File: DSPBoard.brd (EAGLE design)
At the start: 416 x 128.5 mm, 454 parts, among them IC1 AD1939WBSTZ, IC10 LM833D, IC11 LM833D, IC12 TL074D, IC13 4520D, IC2 24AA1025, IC29 TL074D, IC3 LM4040B10DBZ, IC4 LM833D, IC5 LM833D, IC6 LM833D, IC7 LM833D, IC8 LM833D, IC9 LM833D, U1 LM11173.3NOPB, U2 PEC11R-4315F-N0012, U3 PEC11R-4315F-N0012, X1 2510-, Y1 12.288MHz

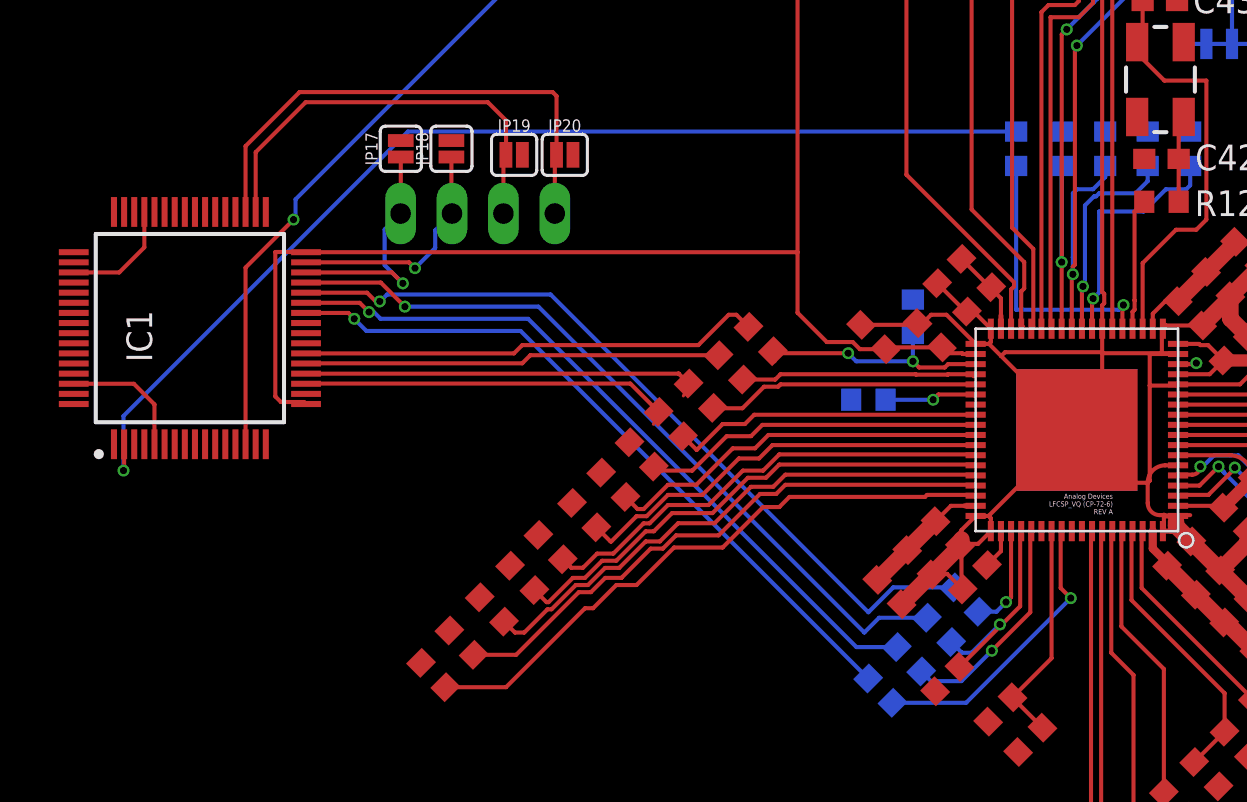
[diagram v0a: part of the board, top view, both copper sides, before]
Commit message: rerouteclockreccomendataions
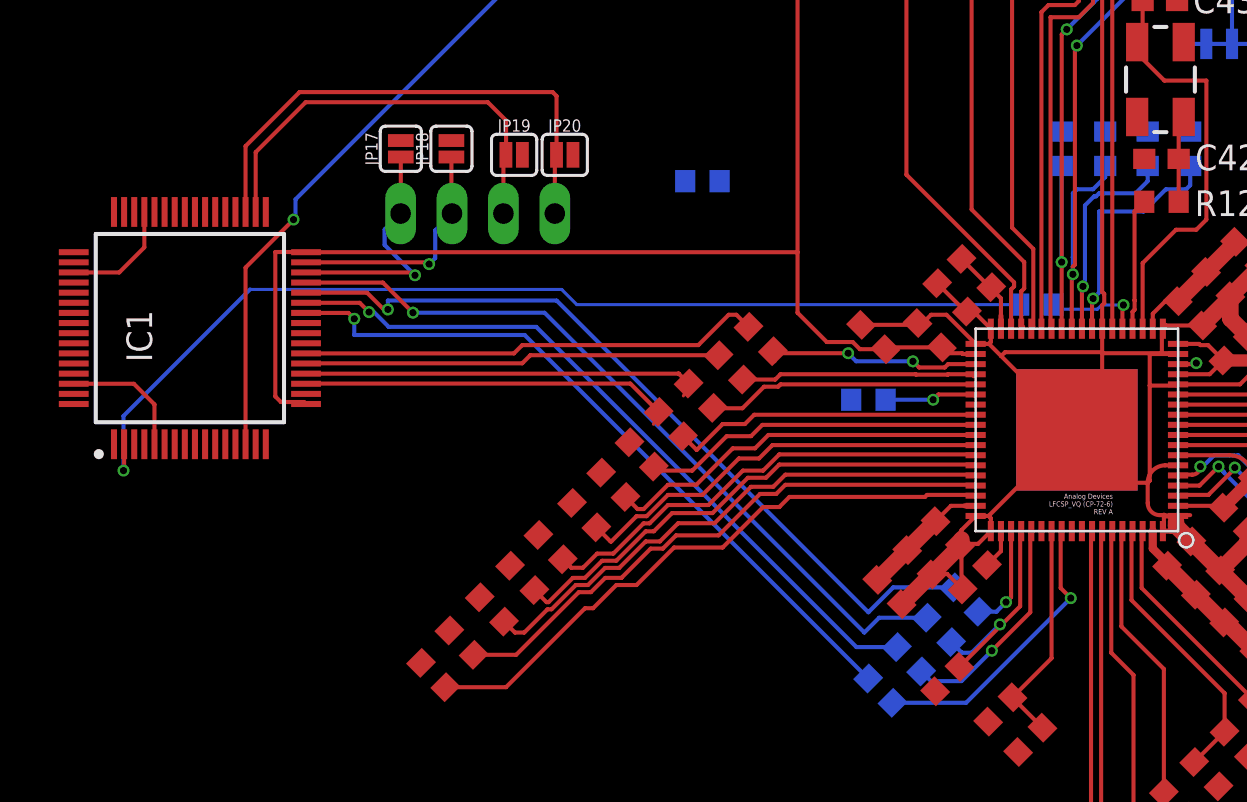
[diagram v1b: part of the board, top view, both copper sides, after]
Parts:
- moved R170 12.4 mm to (189.3, 74.0), turned to 180 degrees
- moved R180 7.76 mm to (205.8, 67.9), turned to 0 degrees
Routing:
- net N$141: track 13.7 -> 4.82 mm
- net 1452_CLK_OUT: track 53.9 -> 51.2 mm
- net MP4: track 12.4 -> 11.0 mm

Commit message: relayingThechips
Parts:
- moved R155 68.9 mm to (108.3, 36.5), turned to 90 degrees
- moved R154 68.5 mm to (110.4, 36.6), turned to 90 degrees
- moved R56 68.2 mm to (112.7, 36.7), turned to 90 degrees
- moved R26 67.9 mm to (114.8, 36.8), turned to 90 degrees
- moved R25 67.7 mm to (116.9, 36.8), turned to 90 degrees
- moved R24 67.5 mm to (119.2, 36.8), turned to 90 degrees
- moved R167 67.4 mm to (121.3, 36.8), turned to 270 degrees
- moved R175 54.8 mm to (152.6, 28.6), turned to 90 degrees
- moved R156 54.4 mm to (154.7, 28.6), turned to 270 degrees
- moved R161 54.1 mm to (156.8, 28.6), turned to 90 degrees
- moved R176 53.8 mm to (159.0, 28.6), turned to 90 degrees
- moved R159 53.6 mm to (161.1, 28.7), turned to 270 degrees
- moved R157 53.4 mm to (163.3, 28.7), turned to 270 degrees
- moved R160 53.3 mm to (165.4, 28.7), turned to 90 degrees
- moved R158 53.1 mm to (167.5, 28.8), turned to 270 degrees
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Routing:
- net N$28: track 21.5 -> 206.3 mm
- net MP0: track 11.9 -> 75.9 mm, vias 1 -> 0
- net +3V3: track 124.0 -> 64.0 mm
- net S_SDA: track 50.6 -> 104.6 mm
- net 1452_CLK_OUT: track 51.2 -> 0.29 mm, vias 1 -> 0
- net N$27: track 6.51 -> 55.8 mm
- net RESET: track 108.1 -> 59.3 mm, vias 2 -> 1
- net ASDATA2: track 35.7 -> 4.18 mm, vias 1 -> 0
- net ALRCLK: track 38.1 -> 10.3 mm
- net ABCLK: track 39.7 -> 13.1 mm
- net S_AUX_ADC1: track 27.9 -> 54.3 mm
- net N$134: track 30.2 -> 3.83 mm
- net ASDATA1: track 36.2 -> 10.3 mm, vias 1 -> 0
- net N$132: track 28.3 -> 4.23 mm
- net S_AUX_ADC0: track 31.1 -> 54.7 mm
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
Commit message: board update
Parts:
- moved R180 16.7 mm to (175.2, 49.1)
- moved R8 14.2 mm to (165.2, 55.9)
- moved R6 14.1 mm to (161.3, 55.5)
- moved R7 12.9 mm to (163.3, 55.9)
- moved R11 10.9 mm to (162.3, 52.6)
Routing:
- net 1452_CLK_OUT: track 0.29 -> 30.7 mm, vias 0 -> 1
- net MP10: track 11.3 -> 20.8 mm
- net N$76: track 5.24 -> 13.7 mm
- net N$35: track 14.5 -> 18.6 mm
- net ASDATA1: track 10.3 -> 13.9 mm, vias 0 -> 1
- net N$120: track 11.0 -> 12.7 mm
- net N$141: track 0.32 -> 1.89 mm, vias 0 -> 1
- net ALRCLK: track 10.3 -> 11.3 mm, vias 1 -> 2
- net ASDATA2: track 4.18 -> 3.33 mm, vias 0 -> 1
- net ABCLK: track 13.1 -> 12.9 mm, vias 1 -> 2

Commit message: continuing to layout
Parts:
- removed SV2: (no value), con-lstb:MA04-1
- added TP1, TP2, TP3, TP4: TESTPAD_TPSQTP16R, BeagleBone_Blue_R3:TESTPAD_TP16R
- moved C119 379.8 mm to (152.6, 77.6), flipped to the bottom, turned to 270 degrees
- moved C98 366.6 mm to (345.5, 180.0)
- moved R70 364.8 mm to (347.4, 172.4)
- moved C96 360.8 mm to (344.7, 178.5)
- moved R99 360.8 mm to (337.0, 165.8)
- moved C52 360.8 mm to (324.3, 165.8)
- moved C63 360.8 mm to (318.0, 165.8)
- moved C67 360.8 mm to (330.7, 159.4)
- moved C74 360.8 mm to (311.6, 165.8)
- moved C78 360.8 mm to (318.0, 159.4)
- moved C83 360.8 mm to (311.6, 159.4)
- moved R72 360.8 mm to (330.7, 172.1)
- moved R73 360.8 mm to (324.3, 172.1)
- moved R74 360.8 mm to (318.0, 172.1)
- moved R76 360.8 mm to (311.6, 172.1)
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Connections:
- net +3V3: no longer D1.1, D2.2, D3.1, D4.2, D5.1, D6.2, D7.1, D8.2
- net 3V3A: now also D1.1, D2.2, D3.1, D4.2, D5.1, D6.2, D7.1, D8.2
- net N$135: now also TP4.TP; no longer SV2.1
- net N$158: now also TP3.TP; no longer SV2.2
- net N$159: now also TP2.TP; no longer SV2.3
- net N$7: now also TP1.TP; no longer SV2.4
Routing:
- net N$28: track 206.3 -> 9.04 mm
- net AIN0+: track 0.00 -> 111.1 mm, vias 0 -> 1
- net AIN0-: track 0.00 -> 108.7 mm, vias 0 -> 1
- net S_SDA: track 104.6 -> 2.01 mm, vias 0 -> 1
- net MP0: track 75.9 -> 12.8 mm, vias 0 -> 1
- net S_AUX_ADC0: track 54.7 -> 7.85 mm
- net S_AUX_ADC1: track 54.3 -> 7.51 mm
- net RESET: track 59.3 -> 103.5 mm, vias 1 -> 2
- net GND: track 217.6 -> 261.5 mm, vias 10 -> 35
- net +3V3: track 64.0 -> 107.2 mm, vias 3 -> 5
- net S_SCL: track 39.9 -> 1.46 mm, vias 0 -> 1
- net N$27: track 55.8 -> 17.9 mm
- net 3V3A: track 0.00 -> 28.0 mm, vias 0 -> 2
- net N$134: track 3.83 -> 15.9 mm, vias 0 -> 1
- net N$132: track 4.23 -> 15.4 mm, vias 0 -> 1
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
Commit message: MAybe I need to rethink this
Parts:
- removed C100, C102, C103, C104, C106, C99: 1nf, rcl:C0603
- removed C101, C105, C56: 10nF, rcl:C0603
- removed C107, C108: 100nF, rcl:C0603
- removed C17, C25: 100nf, rcl:C0603
- removed C50: 220uF, rcl:PANASONIC_D
- removed C51: 1nF, rcl:C0603
- removed C52: 470p, rcl:C0603
- removed C53: 1uF, rcl:C0603
- removed C54: 100uF, rcl:PANASONIC_D
- removed C55: 100pF, rcl:C0603
- removed D3, D4, D7, D8: BAV99,215, SamacSys_Parts:SOT95P230X110-3N
- removed IC10, IC5: LM833D, linear:SO08
- removed JP10, JP14, JP15, JP16, JP4, JP5, JP6, JP7, JP8, JP9: JUMPER-SMT_2_NC_PASTE_SILK, SparkFun-Jumpers:SMT-JUMPER_2_NC_PASTE_SILK
- removed R103, R114: 100R, rcl:R0603
- removed R104, R106, R115, R117, R118, R120, R121, R123, R67: 2.2k, rcl:R0603
- removed R105, R116, R119, R122: 68R, rcl:R0603
- removed R164, R165, R166, R167, R168, R169, R170, R171, R172, R173, R174, R175, R176, R53: 33R, rcl:R0603
- removed R183, R184, R185: 100, rcl:R0603
- removed R46: 6k2, rcl:R0603
- removed R47, R48: 22R, rcl:R0603
- removed R49: 18k, rcl:R0603
- removed TP1, TP2, TP3, TP4: TESTPAD_TPSQTP16R, BeagleBone_Blue_R3:TESTPAD_TP16R
- removed U$14, U$15, U$7: WQP-PJ301M-12_JACK, thonkiconn:WQP-PJ301M-12_JACK
- removed U$24: PHOTON_SMD, Particle-Devices:PHOTON_SMD
- added C133, C180: 1nF, rcl:C0603
- added C156, C181: 470p, rcl:C0603
- added C162, C182: 1uF, rcl:C0603
- added C163, C183: 100uF, rcl:PANASONIC_D
- added C164, C166, C184, C186: 100pF, rcl:C0603
- added C165, C185, C69: 10nF, rcl:C0603
- added C177, C178, C58: 100nf, rcl:C0603
- added C179: 220uF, rcl:PANASONIC_D
- added D10, D13, D14, D9: BAV99,215, SamacSys_Parts:SOT95P230X110-3N
- added IC14, IC16: LM833D, linear:SO08
- added LED1, LED2, LED3, LED4, LED5, LED6, LED7, LED8: (no value), led:CHIPLED_0805
- added R186, R208: 18k, rcl:R0603
- added R187, R209: 2.7k, rcl:R0603
- added R188, R189, R210, R211: 2.2k, rcl:R0603
- added R190, R212: 12.7k, rcl:R0603
- added R191, R192, R213, R214: 10k, rcl:R0603
- added R193, R215: 6k2, rcl:R0603
- added R194, R195, R216, R217: 22R, rcl:R0603
- added R196, R218: 100, rcl:R0603
- added U$22, U$30, U$31: WQP-PJ301M-12_JACK, thonkiconn:WQP-PJ301M-12_JACK
- C132: value 100pF -> 220uF; device rcl:C0603 -> rcl:PANASONIC_D
- C57, C77: value 100pF -> 100nf
- C59: value 100nf -> 220uF; device rcl:C0603 -> rcl:PANASONIC_D
- C60: value 100nf -> 1nF
- C61: value 220uF -> 470p; device rcl:PANASONIC_D -> rcl:C0603
- C62: value 1nF -> 1uF
- C63: value 470p -> 100uF; device rcl:C0603 -> rcl:PANASONIC_D
- C64: value 1uF -> 100pF
- C65: value 100uF -> 10nF; device rcl:PANASONIC_D -> rcl:C0603
- C67, C93: value 10nF -> 1nf
- C68: value 100pF -> 1nf
- C70, C71: value 100nf -> 1nf
- C72: value 220uF -> 1nf; device rcl:PANASONIC_D -> rcl:C0603
- C73: value 1nF -> 10nF
- C74: value 470p -> 1nf
- C75: value 1uF -> 100nF
- C76: value 100uF -> 100nF; device rcl:PANASONIC_D -> rcl:C0603
- C78: value 10nF -> 100nf
- C79, C80: value 100nF -> 1nf
- C91, C95: value 1nf -> 10nF
- C96: device rcl:C0805 -> rcl:C0603
- C97: value 10nF -> 100nF
- C98: value 1nf -> 100nF; device rcl:C0805 -> rcl:C0603
- R15: value 18k -> 33R
- R154: value 33R -> 100R
- R155, R159, R160, R163: value 33R -> 2.2k
- R158, R161: value 33R -> 68R
- R25: value 33R -> 10k
- R26, R29: value 33R -> 470
- R30: value 2.7k -> 470
- R32, R42: value 2.2k -> 470
- R43: value 12.7k -> 470
- R44, R45: value 10k -> 470
- R50: value 2.7k -> 18k
- R51: value 2.2k -> 2.7k
- R55, R69: value 12.7k -> 2.2k
- R57: value 10k -> 12.7k
- R62: value 6k2 -> 10k
- R63: value 22R -> 6k2
- R65: value 18k -> 22R
- R66: value 2.7k -> 100
- R68: value 2.2k -> 100R
- R70: value 10k -> 68R
- R71: value 10k -> 2.2k
- R72: value 6k2 -> 2.2k
- R73: value 22R -> 68R
- R74: value 22R -> 2.2k
- U$29: value PROTOTYPEAREA -> WQP-PJ301M-12_JACK; device audioic:PROTOTYPEAREA -> thonkiconn:WQP-PJ301M-12_JACK
- U$5: value WQP-PJ301M-12_JACK -> PHOTON_WITH_HEADERS; device thonkiconn:WQP-PJ301M-12_JACK -> Particle-Devices:PHOTON
- moved JP1 594.2 mm to (-217.9, -133.8)
- moved JP3 520.5 mm to (-226.5, -133.8), flipped to the top, turned to 0 degrees
- moved R45 472.1 mm to (226.5, -84.6)
- moved R44 464.1 mm to (226.5, -79.7)
- moved R15 425.2 mm to (276.1, -40.5)
- moved R42 418.8 mm to (226.5, -69.9)
- moved C95 409.9 mm to (174.7, 86.4), flipped to the bottom
- moved C94 407.2 mm to (177.9, 89.9), flipped to the bottom
- moved R95 401.2 mm to (169.6, 88.3), flipped to the bottom
- moved C110 397.1 mm to (192.6, 89.9), flipped to the bottom, turned to 180 degrees
- moved R32 395.8 mm to (226.5, -65.0)
- moved R93 395.6 mm to (168.9, 83.7), flipped to the bottom, turned to 90 degrees
- moved C92 393.7 mm to (169.9, 93.3), flipped to the bottom, turned to 180 degrees
- moved R153 390.7 mm to (194.4, 54.4), turned to 180 degrees
- moved C91 388.9 mm to (167.9, 86.2), flipped to the bottom, turned to 180 degrees
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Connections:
- removed net !RST: JP1.2, U$24.23, U$29.P$29
- removed net MP12: R156.1, R161.2, U$1.66
- removed net MP13: R157.1, R160.2, U$1.69
- removed net MP8: JP15.2, R166.2
- removed net MP9: JP16.2, R165.2
- removed net MUX1_X: JP3.2, JP9.1, MUX1.3, U$29.USER_PAD1237
- removed net MUX2_A_INH: MUX2.6, U$29.USER_PAD1249
- removed net MUX2_A_X: JP10.1, JP8.2, MUX2.3, U$29.USER_PAD1250
- removed net MUX2_A_X0: MUX2.13, U$29.USER_PAD1251
- removed net MUX2_A_X1: MUX2.14, U$29.USER_PAD1252
- removed net MUX2_A_X2: MUX2.15, U$29.USER_PAD1253
- removed net MUX2_A_X3: MUX2.12, U$29.USER_PAD1254
- removed net MUX2_A_X4: MUX2.1, U$29.USER_PAD1255
- removed net MUX2_A_X5: MUX2.5, U$29.USER_PAD1256
- removed net MUX2_A_X6: MUX2.2, U$29.USER_PAD1257
- removed net MUX2_A_X7: MUX2.4, U$29.USER_PAD1258
- removed net N$100: C141.1, IC11.5, R129.2
- removed net N$101: C138.2, R124.2, U$15.P$1
- removed net N$102: C109.2, R103.2, U$14.P$1
- removed net N$103: C110.1, IC11.1, R103.1, R104.2
- removed net N$140: R25.1, U$1.48
- removed net N$143: R160.1, U$29.P$28
- removed net N$144: R161.1, U$29.P$27
- removed net N$145: R163.1, U$29.P$26
- removed net N$146: R164.1, U$29.P$25
- removed net N$147: R165.1, U$29.P$24
- removed net N$148: R166.1, U$29.P$23
- removed net N$149: R167.1, U$29.P$22
- removed net N$150: R168.1, U$29.P$21
- removed net N$151: R169.1, U$29.P$20
- removed net N$152: R170.1, U$29.P$19
- removed net N$153: R171.1, U$29.P$18
- removed net N$154: R172.1, U$29.P$17
- removed net N$155: R173.1, U$29.P$16
- removed net N$156: R174.1, U$29.P$15
- removed net N$161: R185.2, R46.1
- removed net N$162: R183.2, R62.1
- removed net N$163: R184.2, R72.1
- removed net N$98: C140.2, R128.2, R129.1, R130.2
- removed net N$99: C139.1, IC11.7, R124.1, R125.2
- removed net P_ADC0: U$24.12, U$29.P$36
- removed net P_ADC1: U$24.11, U$29.P$37
- removed net P_ADC2: U$24.10, U$29.P$38
- removed net P_ADC3: U$24.9, U$29.P$39
- removed net P_ADC4: U$24.8, U$29.P$40
- removed net P_ADC5: U$24.7, U$29.P$41
- removed net P_ADC6_DAC: U$24.6, U$29.P$42
- removed net P_ADC7_WPK: U$24.5, U$29.P$43
- removed net P_D0: U$24.13, U$29.P$3
- removed net P_D1: U$24.14, U$29.P$4
- removed net P_D2: U$24.15, U$29.P$5
- removed net P_D3: U$24.16, U$29.P$6
- removed net P_D4: U$24.17, U$29.P$7
- removed net P_D5: U$24.18, U$29.P$8
- removed net P_D6: U$24.19, U$29.P$9
- removed net P_D7: U$24.20, U$29.P$10
- removed net RX: U$24.4, U$29.P$12
- removed net SDATA_IN2_BCLK: R175.1, U$29.USER_PAD1291
- removed net SDATA_IN2_DATA: R176.1, U$29.USER_PAD1292
- removed net SDATA_IN2_LRCLK: R156.2, U$29.USER_PAD1293
- removed net SDATA_IN3_BCLK: R159.2, U$29.USER_PAD1288
- removed net SDATA_IN3_DATA: R158.2, U$29.USER_PAD1289
- removed net SDATA_IN3_LRCLK: R157.2, U$29.USER_PAD1290
- removed net SDATA_OUT2_BCLK: R25.2, U$29.USER_PAD1297
- removed net SDATA_OUT2_DATA: R26.2, U$29.USER_PAD1298
- removed net SDATA_OUT2_LRCLK: IC13.1, IC13.9, R24.2, U$29.USER_PAD1299
- removed net SDATA_OUT3_BCLK: R154.2, U$29.USER_PAD1294
- removed net SDATA_OUT3_DATA: R155.2, U$29.USER_PAD1295
- removed net SDATA_OUT3_LRCLK: R56.2, U$29.USER_PAD1296
- removed net SEL0: R27.2, R59.2
- removed net S_AUX_ADC0: JP3.1, U$1.8, U$29.P$44
- removed net S_AUX_ADC1: JP4.1, U$1.9, U$29.P$45
- removed net S_AUX_ADC2: JP5.1, U$1.10, U$29.P$46
- removed net S_AUX_ADC3: JP6.1, U$1.11, U$29.P$47
- removed net S_AUX_ADC4: JP7.1, U$1.12, U$29.P$48
- removed net S_AUX_ADC5: JP8.1, U$1.13, U$29.P$49
- removed net TX: U$24.3, U$29.P$11
- new net AUXADC0: MUX1.3, U$1.8
- new net AUXADC1: U$1.9
- new net AUXADC3: U$1.11
- new net AUXADC4: U$1.12
- new net AUXADC5: U$1.13
- new net ENCODER0_2: U$1.10
- new net LED_DRIVE: MUX2.3, R27.2
- new net MUX1_ENABLE1: MUX2.6, R25.2
- new net MUX_CLK: IC13.1, IC13.9, R15.2
- new net N$168: C133.1, R186.2, R187.1, R193.2
- new net N$169: C156.2, IC14.3, R187.2
- new net N$170: C133.2, IC14.1, IC14.2, R188.2, R195.2
- new net N$171: IC14.6, R188.1, R189.2
- new net N$172: IC14.7, R189.1, R194.2
- new net N$173: C162.2, IC14.5, R190.1
- new net N$174: C162.1, C163.+, R190.2, R191.2, R192.1, R196.1
- new net N$175: C132.-, U$22.P$1
- new net N$176: C132.+, R186.1
- new net N$177: R193.1, R196.2
- new net N$188: C180.1, R208.2, R209.1, R215.2
- new net N$189: C181.2, IC16.3, R209.2
- new net N$190: C180.2, IC16.1, IC16.2, R210.2, R217.2
- new net N$191: IC16.6, R210.1, R211.2
- new net N$192: IC16.7, R211.1, R216.2
- new net N$193: C182.2, IC16.5, R212.1
- new net N$194: C182.1, C183.+, R212.2, R213.2, R214.1, R218.1
- new net N$195: C179.-, U$31.P$1
- new net N$196: C179.+, R208.1
- new net N$197: R215.1, R218.2
- net +12V: now also C177.1, C57.1, C76.2, C77.1, C98.2, IC14.8, IC16.8; no longer C108.2, C17.1, C59.1, C70.1, C80.2, IC10.8, IC5.8, U$29.P$51
- net +3V3: now also R25.1, U$5.24; no longer U$24.24, U$29.P$56
- net +5V: no longer U$29.P$55
- net -12V: now also C178.2, C58.2, C75.1, C78.2, C97.1, IC14.4, IC16.4; no longer C107.1, C25.2, C60.2, C71.2, C79.1, IC10.4, IC5.4, U$29.P$52
- net 3V3A: now also D10.2, D13.1, D14.2, D9.1, R192.2, R214.2, R62.2; no longer D3.1, D4.2, D7.1, D8.2, R45.2, R61.2, R71.2, U$29.P$53
- net AIN1+: now also C65.2, C66.1, D6.3, R64.1; no longer C56.2, C57.1, D4.3, R47.1
- net AIN1-: now also C64.2, C65.1, D5.3, R65.1; no longer C55.2, C56.1, D3.3, R48.1
- net AIN2+: now also C165.2, C166.1, D10.3, R194.1; no longer C67.2, C68.1, D7.3, R63.1
- net AIN2-: now also C164.2, C165.1, D9.3, R195.1; no longer C66.2, C67.1, D8.3, R64.1
- net AIN3+: now also C185.2, C186.1, D14.3, R216.1; no longer C132.1, C78.2, D6.3, R73.1
- net AIN3-: now also C184.2, C185.1, D13.3, R217.1; no longer C77.2, C78.1, D5.3, R74.1
- net AOUT0+: now also R72.1; no longer R111.1
- net AOUT0-: now also R71.1; no longer R110.1
- net AOUT1+: now also R111.1; no longer R118.1
- net AOUT1-: now also R110.1; no longer R117.1
- net AOUT6+: now also R128.1; no longer R121.1
- net AOUT6-: now also R127.1; no longer R106.1
- net AOUT7+: now also R160.1; no longer R128.1
- net AOUT7-: now also R159.1; no longer R127.1
- net CV0: no longer U$29.USER_PAD1238
- net CV1: no longer U$29.USER_PAD1239
- net CV2: no longer U$29.USER_PAD1240
- net CV3: no longer U$29.USER_PAD1241
- net CV4: no longer U$29.USER_PAD1242
- net CV5: no longer U$29.USER_PAD1243
- net CV6: no longer U$29.USER_PAD1244
- net CV7: no longer U$29.USER_PAD1245
- net DSP_47: no longer JP15.1
- net DSP_50: no longer JP16.1
- net ENCODER0_0: now also R157.2; no longer JP4.2
- net ENCODER0_1: now also R156.2; no longer JP5.2
- net ENCODER1_0: now also R56.2; no longer JP6.2
- net ENCODER1_1: now also R24.2; no longer JP7.2
- net GND: now also C156.1, C163.-, C164.1, C166.2, C177.2, C178.1, C181.1, C183.-, C184.1, C186.2, C58.1, C61.1, C63.-, C64.1, C66.2, C67.1, C74.2, C75.2, C76.1, C77.2, C78.1, C79.1, C92.2, C93.1, C96.2, C97.2, C98.1, D10.1, D13.2, D14.1, D9.2, R163.1, R191.1, R213.1, R26.1, R29.1, R30.1, R32.1, R42.1, R43.1, R45.1, R61.1, R74.1, U$22.P$2, U$22.P$3, U$29.P$2, U$29.P$3, U$30.P$2, U$30.P$3, U$31.P$2, U$31.P$3, U$5.2, U$5.21; no longer C102.2, C103.1, C106.2, C107.2, C108.1, C132.2, C17.2, C25.1, C52.1, C54.-, C55.1, C59.2, C60.1, C63.1, C65.-, C66.1, C68.2, C74.1, C76.-, C77.1, C79.2, C80.1, C91.1, C94.2, C95.1, C98.2, C99.1, D3.2, D4.1, D7.2, D8.1, R120.1, R123.1, R57.1, R70.1, U$14.P$2, U$14.P$3, U$15.P$2, U$15.P$3, U$24.2, U$24.21, U$29.P$35, U$29.P$50, U$29.P$54, U$29.USER_PAD1232, U$29.USER_PAD1287, U$5.P$2, U$5.P$3, U$7.P$2, U$7.P$3
- net MP0: no longer R174.2
- net MP1: no longer R173.2
- net MP10: no longer R164.2
- net MP11: no longer R163.2
- net MP2: no longer R172.2
- net MP3: no longer R171.2
- net MP4: no longer JP14.1, JP14.2, R170.2
- net MP5: no longer R169.2
- net MP6: no longer R168.2
- net MP7: no longer R167.2
- net MUX1_A: no longer U$29.USER_PAD1233
- net MUX1_B: no longer U$29.USER_PAD1234
- net MUX1_C: no longer U$29.USER_PAD1235
- net MUX1_ENABLE: no longer U$29.USER_PAD1236
- net MUX2_A_A: no longer U$29.USER_PAD1246
- net MUX2_A_B: no longer U$29.USER_PAD1247
- net MUX2_A_C: no longer U$29.USER_PAD1248
- net N$104: now also C139.2, IC11.6, R158.2; no longer C110.2, IC11.2, R105.2
- net N$105: now also C140.1, R155.1, R158.1, R159.2; no longer C134.1, R104.1, R105.1, R106.2
- net N$106: now also C140.2, R160.2, R161.1, R163.2; no longer C134.2, R121.2, R122.1, R123.2
- net N$107: now also C139.1, IC11.7, R154.1, R155.2; no longer C135.1, IC11.3, R122.2
- net N$123: now also C141.1, IC11.5, R161.2; no longer R29.2, U$29.P$13
- net N$126: now also C138.2, R154.2, U$30.P$1; no longer R53.2, U$29.P$14
- net N$130: now also C109.2, R124.2, U$29.P$1; no longer R158.1, U$1.70
- net N$132: now also C110.1, IC11.1, R124.1, R125.2; no longer R154.1, U$1.51
- net N$134: now also C110.2, IC11.2, R126.2; no longer R155.1, U$1.52
- net N$135: no longer JP20.1, TP4.TP
- net N$136: now also C134.1, R125.1, R126.1, R127.2; no longer JP10.2
- net N$137: now also C134.2, R128.2, R129.1, R130.2; no longer JP9.2
- net N$139: now also C135.1, IC11.3, R129.2; no longer R26.1, U$1.49
- net N$158: no longer JP19.1, TP3.TP
- net N$159: no longer TP2.TP
- net N$17: now also LED1.A, MUX2.13; no longer C100.2, IC10.6, R116.2
- net N$19: now also R156.1, U$1.66; no longer C51.1, R15.2, R30.1, R46.2
- net N$20: now also R157.1, U$1.69; no longer C52.2, IC5.3, R30.2
- net N$22: now also LED2.A, MUX2.14; no longer C101.1, R115.1, R116.1, R117.2
- net N$23: now also JP20.1; no longer C51.2, IC5.1, IC5.2, R32.2, R48.2
- net N$25: now also JP19.1; no longer IC5.6, R32.1, R42.2
- net N$26: now also LED3.A, MUX2.15; no longer IC5.7, R42.1, R47.2
- net N$30: now also LED4.A, MUX2.12; no longer R175.2, U$1.65
- net N$33: now also LED5.A, MUX2.1; no longer R159.1, U$1.68
- net N$34: now also LED6.A, MUX2.5; no longer C53.2, IC5.5, R43.1
- net N$36: now also LED7.A, MUX2.2; no longer C53.1, C54.+, R185.1, R43.2, R44.2, R45.1
- net N$38: now also LED8.A, MUX2.4; no longer C50.-, U$5.P$1
- net N$39: now also LED1.C, R45.2; no longer R176.2, U$1.67
- net N$40: now also LED2.C, R44.2; no longer C50.+, R15.1
- net N$41: now also LED3.C, R43.2; no longer C62.1, R49.2, R50.1, R62.2
- net N$42: now also C60.1, R51.1, R63.2; no longer C63.2, IC6.3
- net N$43: now also C61.2, IC6.3; no longer C62.2, IC6.1, IC6.2, R64.2
- net N$44: now also C60.2, IC6.1, IC6.2, R65.2; no longer IC6.6, R51.1
- net N$45: now also IC6.6, R55.2; no longer IC6.7, R63.2
- net N$46: now also IC6.7, R64.2; no longer C64.2, IC6.5
- net N$47: now also C62.2, IC6.5, R57.1; no longer C64.1, C65.+, R183.1, R55.2, R57.2, R61.1
- net N$48: now also C62.1, C63.+, R57.2, R61.2, R62.1, R66.1; no longer C61.-, U$6.P$1
- net N$49: now also C59.-, U$6.P$1; no longer C61.+, R49.1
- net N$50: now also C59.+, R50.1; no longer C73.1, R65.2, R66.1, R72.2
- net N$51: now also R63.1; no longer C74.2, IC7.3
- net N$52: now also LED4.C, R42.2; no longer C73.2, IC7.1, IC7.2, R67.2, R74.2
- net N$53: now also C72.2, R109.2; no longer R67.1, R68.2
- net N$54: now also C73.1, R108.1, R109.1, R110.2; no longer IC7.7, R68.1, R73.2
- net N$55: now also C73.2, R111.2, R112.1, R113.2; no longer C75.2, IC7.5, R69.1
- net N$56: now also C72.1, IC7.7, R107.1, R108.2; no longer C75.1, C76.+, R184.1, R69.2, R70.2, R71.1
- net N$57: now also C74.1, IC7.5, R112.2; no longer C72.-, U$7.P$1
- net N$58: now also C71.2, R107.2, U$17.P$1; no longer C72.+, R65.1
- net N$59: now also C67.2, R68.2, U$16.P$1; no longer C101.2, R118.2, R119.1, R120.2
- net N$60: now also C68.1, IC7.1, R68.1, R69.2; no longer C100.1, IC10.7, R114.1, R115.2
- net N$61: now also C68.2, IC7.2, R70.2; no longer C102.1, IC10.5, R119.2
- net N$62: now also C69.1, R69.1, R70.1, R71.2; no longer C99.2, R114.2, U$17.P$1
- net N$63: now also C69.2, R72.2, R73.1, R74.2; no longer C95.2, R107.2, U$16.P$1
- net N$64: now also C70.1, IC7.3, R73.2; no longer C96.1, IC10.1, R107.1, R108.2
- net N$65: now also C94.2, IC9.6, R98.2; no longer C96.2, IC10.2, R109.2
- net N$66: now also C95.1, R97.1, R98.1, R99.2; no longer C97.1, R108.1, R109.1, R110.2
- net N$67: now also C95.2, R100.2, R101.1, R102.2; no longer C97.2, R111.2, R112.1, R113.2
- net N$68: now also C94.1, IC9.7, R96.1, R97.2; no longer C98.1, IC10.3, R112.2
- net N$7: no longer TP1.TP
- net N$84: now also C96.1, IC9.5, R101.2; no longer C104.2, IC9.6, R98.2
- net N$85: now also C93.2, R96.2, U$13.P$1; no longer C105.1, R97.1, R98.1, R99.2
- net N$86: now also C79.2, R89.2, U$12.P$1; no longer C105.2, R100.2, R101.1, R102.2
- net N$87: now also C80.1, IC9.1, R89.1, R90.2; no longer C104.1, IC9.7, R96.1, R97.2
- net N$88: now also C80.2, IC9.2, R91.2; no longer C106.1, IC9.5, R101.2
- net N$89: now also C91.1, R90.1, R91.1, R92.2; no longer C103.2, R96.2, U$13.P$1
- net N$90: now also R93.2, R94.1, R95.2; no longer R89.2, U$12.P$1
- net N$91: now also IC9.3, R94.2; no longer IC9.1, R89.1, R90.2
- net N$92: now also LED5.C, R32.2; no longer C92.2, IC9.2, R91.2
- net N$93: now also LED6.C, R30.2; no longer C93.1, R90.1, R91.1, R92.2
- net N$94: now also LED7.C, R29.2; no longer C93.2, R93.2, R94.1, R95.2
- net N$95: now also LED8.C, R26.2; no longer C94.1, IC9.3, R94.2
- net N$96: now also JP1.1, U$5.14; no longer C139.2, IC11.6, R126.2
- net N$97: now also JP3.1, U$5.13; no longer C140.1, R125.1, R126.1, R127.2
- net RESET: now also U$5.23; no longer JP1.1
- net SW0: now also R59.2
- net S_SCL: now also JP1.2; no longer R29.1
- net S_SDA: now also JP3.2; no longer R53.1
- net VBAT: now also U$5.22; no longer U$24.22, U$29.P$2
- net VIN: now also U$5.1; no longer U$24.1, U$29.P$1
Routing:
- net AOUT7-: track 0.00 -> 109.9 mm
- net AOUT0-: track 0.00 -> 109.7 mm
- net AOUT0+: track 0.00 -> 108.4 mm, vias 0 -> 2
- net AOUT7+: track 0.00 -> 108.1 mm
- net AOUT1+: track 0.00 -> 102.7 mm
- net AOUT6+: track 0.00 -> 100.9 mm, vias 0 -> 2
- net AOUT1-: track 0.00 -> 100.0 mm
- net AOUT6-: track 0.00 -> 98.8 mm
- net RESET: track 103.5 -> 16.7 mm
- net AOUT2-: track 0.00 -> 79.3 mm
- net AOUT2+: track 0.00 -> 78.4 mm, vias 0 -> 2
- net AOUT5-: track 0.00 -> 77.7 mm
- net AOUT5+: track 0.00 -> 75.2 mm
- net AOUT3+: track 0.00 -> 72.2 mm
- net AOUT4-: track 0.00 -> 70.7 mm, vias 0 -> 2
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- added copper zone on layer 1, net N$16
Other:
- board size 416 x 128.5 mm -> 213.4 x 110 mm

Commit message: starting to consider making it a 2 board project
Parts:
- moved R155 146.4 mm to (73.6, 25.5), turned to 270 degrees
- moved C138 145.7 mm to (80.6, 23.8), turned to 90 degrees
- moved R159 145.6 mm to (69.7, 27.6), turned to 180 degrees
- moved R154 145.6 mm to (78.1, 24.6), turned to 180 degrees
- moved C139 145.5 mm to (75.6, 25.5), turned to 90 degrees
- moved R160 143.0 mm to (69.7, 29.6), turned to 180 degrees
- moved C140 142.9 mm to (72.1, 28.7), turned to 90 degrees
- moved R158 142.6 mm to (74.6, 28.0), turned to 180 degrees
- moved U$30 142.3 mm to (87.6, 24.8), turned to 270 degrees
- moved R163 139.6 mm to (74.1, 30.5), turned to 270 degrees
- moved R161 139.0 mm to (76.5, 30.0), turned to 180 degrees
- moved IC11 137.7 mm to (73.4, 32.2), turned to 180 degrees
- moved C142 137.4 mm to (69.9, 33.8), turned to 270 degrees
- moved C141 137.2 mm to (79.0, 30.6), turned to 90 degrees
- moved R128 136.8 mm to (69.4, 34.6), turned to 180 degrees
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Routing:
- net AOUT0+: track 108.4 -> 32.9 mm
- net AOUT1+: track 102.7 -> 28.2 mm
- net AOUT0-: track 109.7 -> 35.9 mm, vias 0 -> 2
- net AOUT1-: track 100.0 -> 26.5 mm
- net AOUT7-: track 109.9 -> 36.6 mm
- net AOUT7+: track 108.1 -> 35.9 mm
- net AOUT6-: track 98.8 -> 29.1 mm
- net AOUT6+: track 100.9 -> 31.5 mm
- net AOUT2-: track 79.3 -> 13.0 mm
- net AOUT2+: track 78.4 -> 13.5 mm
- net AOUT5-: track 77.7 -> 14.7 mm
- net AOUT5+: track 75.2 -> 15.1 mm
- net AOUT3+: track 72.2 -> 15.2 mm
- net AOUT3-: track 70.2 -> 15.8 mm
- net AOUT4-: track 70.7 -> 17.5 mm, vias 2 -> 0
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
